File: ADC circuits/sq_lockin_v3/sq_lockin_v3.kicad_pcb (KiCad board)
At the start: 2 copper layers, 100 x 70 mm, 78 parts, among them J1 battery, J10 Conn_01x03_Male, J11 Conn_01x02_Male_2.54mm, J12 Conn_01x02_Male_2.54mm, J13 Conn_01x02_Male_2.54mm, J14 Conn_01x02_Male_2.54mm, J2 Conn_01x02_Male_2.54mm, J21 Conn_01x02_Male_2.54mm, J22 Conn_01x03_Female, J3 DB9_Female_MountingHoles, J4 Conn_01x02_Male_2.54mm, J5 Conn_01x02_Male_2.54mm, J6 receptacle, J7 Conn_01x03_Female, J8 USB_C_KoreanHroparts_6P, J9 receptacle, Q1 BSS84, Q2 2N7002, Q3 BSS84, Q4 2N7002, Q5 BSS84, Q6 2N7002, U10 LMP7715, U11 HX710C, U12 HX710C, U13 AQW212EHAX, U14 AQW212EHAX, U15 KAQY212S, U16 AQW212EHAX, U17 AQW212EHAX, U2 REF3320, U3 LP5907MFX-4.5, U4 LP5907MFX-3.3, U5 LMP7715, U6 LMP7715, U7 AQW212EHAX, U8 AQW212EHAX, U9 LMP7715

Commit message: Add power-two-wre and tweaks to sq_lockin_v3
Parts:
- removed C10, C11: 100nF, Capacitor_SMD:C_0603_1608Metric_Pad1.05x0.95mm_HandSolder
- removed J12, J14: Conn_01x02_Male_2.54mm, Connector_PinHeader_2.54mm:PinHeader_1x02_P2.54mm_Vertical
- removed U10, U9: LMP7715, Package_TO_SOT_SMD:TSOT-23-5
- removed U15: KAQY212S, 0my_footprints:SOP-4_L4.4-W4.0-P2.54-LS7.0-BL
- added C1: 100nF, Capacitor_SMD:C_0603_1608Metric_Pad1.05x0.95mm_HandSolder, F.Cu at (182.1, 102.1)
- added C15: 100nF, Capacitor_SMD:C_0603_1608Metric_Pad1.05x0.95mm_HandSolder, F.Cu at (181.6, 96.6)
- added C16: 100nF, Capacitor_SMD:C_0603_1608Metric_Pad1.05x0.95mm_HandSolder, F.Cu at (193.6, 100.8)
- added C17: 100nF, Capacitor_SMD:C_0603_1608Metric_Pad1.05x0.95mm_HandSolder, F.Cu at (187.5, 107.8)
- added D1: LBAT54HT1G, Diode_SMD:D_SOD-323, F.Cu at (172.2, 71.6)
- added D2: LBAT54HT1G, Diode_SMD:D_SOD-323, F.Cu at (172.2, 69.2)
- added R25: 100, Resistor_SMD:R_0603_1608Metric_Pad1.05x0.95mm_HandSolder, F.Cu at (186.6, 97.0)
- added R26: 10, Resistor_SMD:R_0603_1608Metric_Pad1.05x0.95mm_HandSolder, F.Cu at (190.9, 106.6)
- added R27: 10K, Resistor_SMD:R_0603_1608Metric_Pad1.05x0.95mm_HandSolder, F.Cu at (183.6, 107.8)
- added R28: 10K, Resistor_SMD:R_0603_1608Metric_Pad1.05x0.95mm_HandSolder, F.Cu at (181.4, 110.7)
- added U1: LMP7715, Package_TO_SOT_SMD:TSOT-23-5, F.Cu at (179.5, 104.7)
- added U18: LMP7715, Package_TO_SOT_SMD:TSOT-23-5, F.Cu at (179.5, 99.3)
- added U19: AD623, Package_SO:SOIC-8_3.9x4.9mm_P1.27mm, F.Cu at (188.4, 101.9)
- added U20: LMP7715, Package_TO_SOT_SMD:TSOT-23-5, F.Cu at (185.3, 110.5)
- J3: footprint Connector_Dsub:DSUB-9_Female_Horizontal_P2.77x2.84mm_EdgePinOffset4.94mm_Housed_MountingHolesOffset7.48mm -> 0my_footprints:DSUB-TH_DS1037-09FNAKT74-0CC
- U2: footprint Package_TO_SOT_SMD:SOT-23 -> Package_TO_SOT_SMD:SOT-323_SC-70
- moved J13 71.7 mm to (190.9, 97.0), turned to 90 degrees
- moved Q1 42.6 mm to (159.2, 91.7)
- moved Q2 42.6 mm to (163.6, 91.7)
- moved Q3 31.8 mm to (157.9, 114.9)
- moved Q4 31.8 mm to (162.4, 114.9)
- moved Q6 27.8 mm to (146.9, 104.1), turned to 270 degrees
- moved Q5 24.4 mm to (146.9, 108.0)
- moved C6 13.8 mm to (138.4, 61.0), turned to 90 degrees
- moved J7 9.28 mm to (207.4, 109.6)
- moved U2 9.15 mm to (135.7, 61.0), turned to 90 degrees
- moved J5 7.10 mm to (143.0, 81.4)
- moved C5 5.85 mm to (132.7, 60.9), turned to 90 degrees
- moved C12 5.83 mm to (197.5, 105.6)
- moved C14 5.83 mm to (207.2, 102.6)
- moved C13 5.83 mm to (197.3, 101.5)
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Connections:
- net /sheet624D2E56/in+ renamed /Sheet6275CBF8/in+
- net /sheet624D2E56/in- renamed /Sheet6275CBF8/in-
- C5 pad 2: Net-(C5-Pad2) -> GND
- C6 pad 2: Net-(C5-Pad2) -> GND
- J1 pad 1: Net-(C2-Pad1) -> Net-(D2-Pad2)
- J13 pad 2: /sheet624D2E58/ctrl- -> Net-(J13-Pad2)
- Q1 pad 3: Net-(J12-Pad1) -> /Sheet624B5D4E/ctrl-
- Q2 pad 3: Net-(J12-Pad1) -> /Sheet624B5D4E/ctrl-
- Q3 pad 3: Net-(J13-Pad1) -> /sheet624D2E58/ctrl-
- Q4 pad 3: Net-(J13-Pad1) -> /sheet624D2E58/ctrl-
- Q5 pad 3: Net-(J14-Pad1) -> /sheet6256EE2A/ctrl-
- Q6 pad 3: Net-(J14-Pad1) -> /sheet6256EE2A/ctrl-
- R11 pad 1: Net-(R11-Pad1) -> Net-(J5-Pad2)
- R12 pad 1: Net-(R12-Pad1) -> Net-(J5-Pad1)
- R12 pad 2: Net-(R11-Pad1) -> Net-(J5-Pad2)
- R13 pad 2: Net-(R12-Pad1) -> Net-(J5-Pad1)
- R9 pad 1: Net-(R12-Pad1) -> Net-(J5-Pad1)
- U2 pad 3: Net-(C5-Pad2) -> GND
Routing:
- net VCC: track 69.4 -> 288.1 mm, vias 4 -> 14
- net /vref: track 7.35 -> 155.5 mm, vias 2 -> 5
- net /V-: track 0.27 -> 81.0 mm, vias 0 -> 2
- net /V+: track 0.16 -> 68.3 mm, vias 0 -> 1
- net /I+: track 17.2 -> 78.8 mm, vias 2 -> 3
- net /sheet6256EE2A/ctrl-: track 0.00 -> 54.7 mm
- net /sheet6256EE2A/ctrl+: track 0.00 -> 53.2 mm, vias 0 -> 2
- net +4V: track 10.2 -> 45.6 mm
- net GND: track 72.6 -> 107.3 mm, vias 2 -> 6
- net /Sheet624B5D4E/in+: track 19.6 -> 52.2 mm, vias 2 -> 3
- net /I-: track 3.26 -> 35.8 mm
- net Net-(J3-Pad0): track 0.00 -> 32.0 mm
- net Net-(C4-Pad1): track 28.7 -> 58.8 mm
- net /Sheet6275CBF8/in+: track 0.00 -> 29.9 mm
- net /Sheet621A3D16/in+: track 5.85 -> 31.0 mm
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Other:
- board text added: "sq_lockin_v3 4/2022"
- board text removed: "ADC preamp test CS5530 test 2/2022"

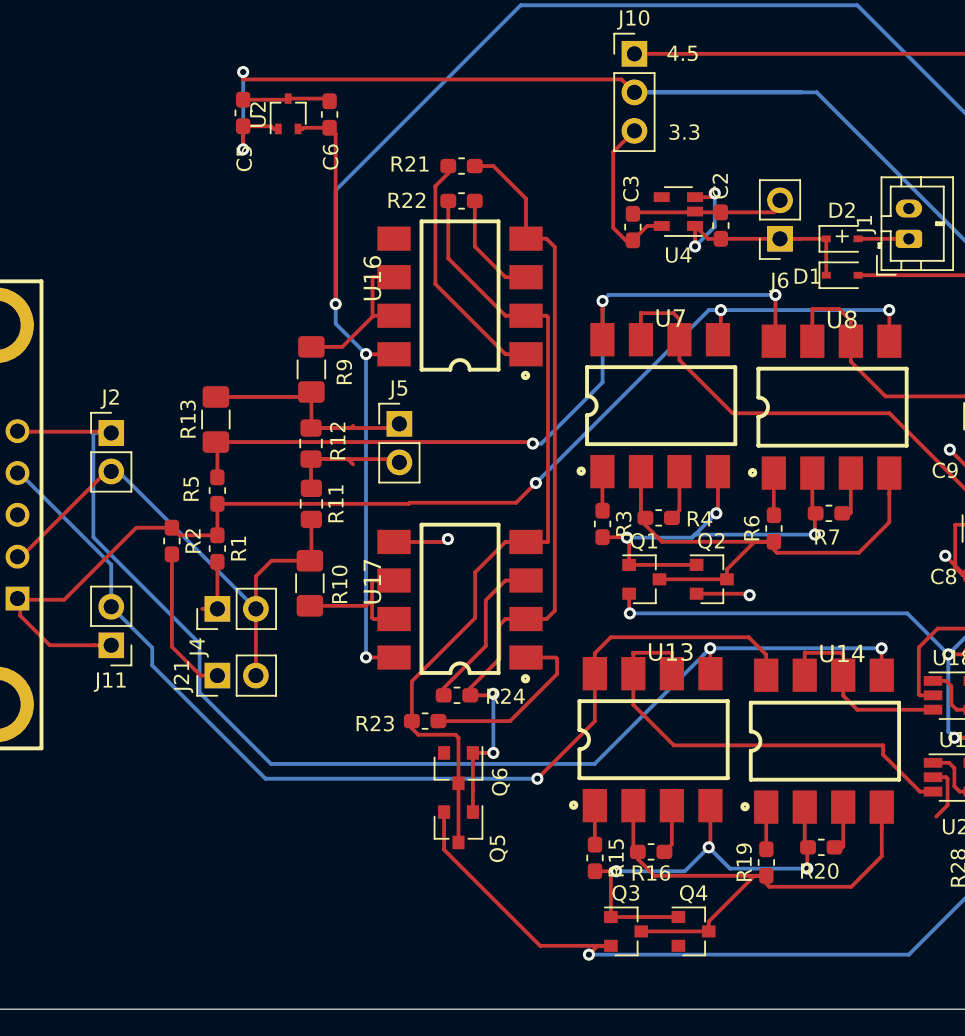
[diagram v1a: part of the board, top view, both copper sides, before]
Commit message: add uart mux versions
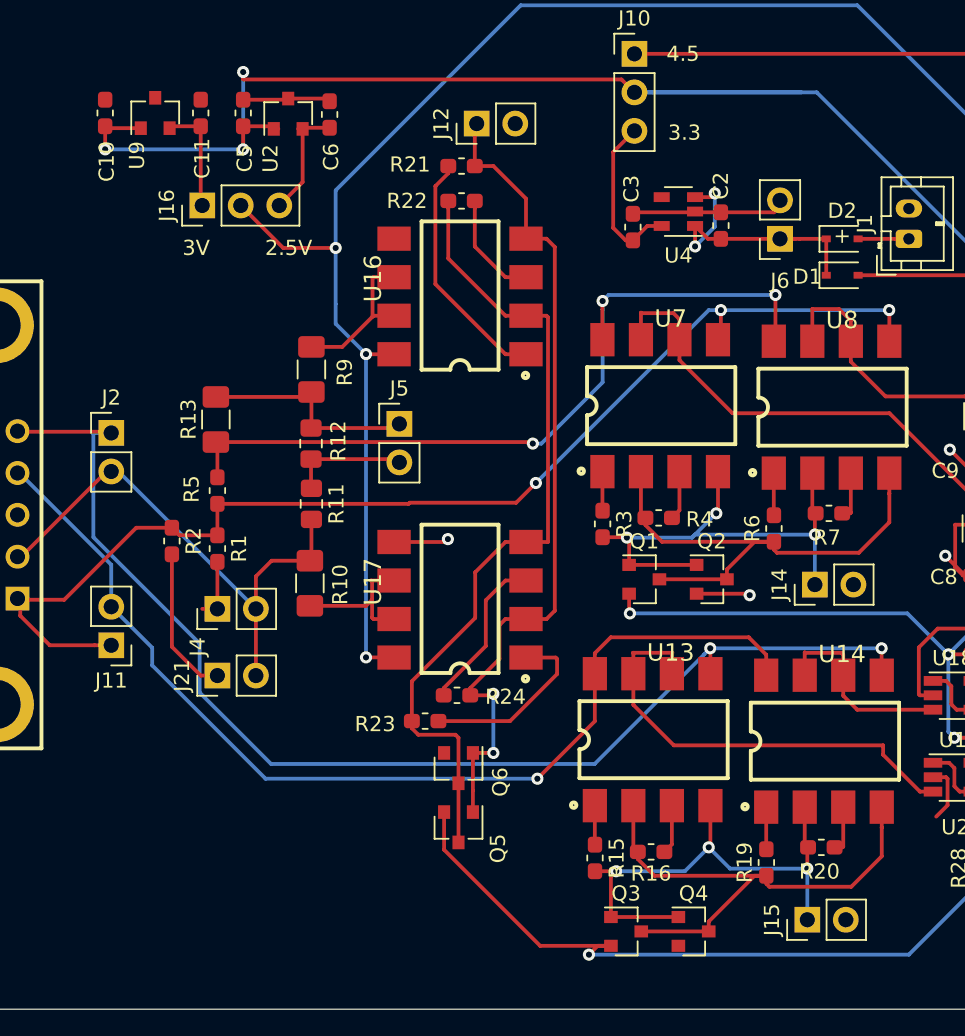
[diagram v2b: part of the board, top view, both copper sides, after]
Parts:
- added C10: 1uF, Capacitor_SMD:C_0603_1608Metric_Pad1.05x0.95mm_HandSolder, F.Cu at (123.6, 60.9)
- added C11: 1uF, Capacitor_SMD:C_0603_1608Metric_Pad1.05x0.95mm_HandSolder, F.Cu at (129.9, 60.9)
- added J12: Conn_01x02_Male_2.54mm, Connector_PinHeader_2.54mm:PinHeader_1x02_P2.54mm_Vertical, F.Cu at (148.1, 61.6)
- added J14: Conn_01x02_Male_2.54mm, Connector_PinHeader_2.54mm:PinHeader_1x02_P2.54mm_Vertical, F.Cu at (170.4, 92.0)
- added J15: Conn_01x02_Male_2.54mm, Connector_PinHeader_2.54mm:PinHeader_1x02_P2.54mm_Vertical, F.Cu at (169.9, 114.1)
- added J16: Conn_01x03_Male, Connector_PinHeader_2.54mm:PinHeader_1x03_P2.54mm_Vertical, F.Cu at (130.0, 67.0)
- added U9: REF3030, Package_TO_SOT_SMD:SOT-23, F.Cu at (126.9, 60.9)
- U2: value REF3320 -> REF3325; footprint Package_TO_SOT_SMD:SOT-323_SC-70 -> Package_TO_SOT_SMD:SOT-23
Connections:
- C6 pad 1: /vref -> /vref1
- U2 pad 2: /vref -> /vref1
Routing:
- net VCC: track 288.1 -> 301.2 mm, vias 14 -> 15
- net /vref1: track 0.00 -> 7.80 mm
- net /vref2: track 0.00 -> 7.37 mm
- net /vref: track 155.5 -> 149.0 mm
- net /sheet624D2E58/ctrl+: track 29.8 -> 33.2 mm
- net /Sheet624B5D4E/ctrl+: track 29.6 -> 32.9 mm
- net Net-(J5-Pad2): track 11.0 -> 8.11 mm
- net /sheet6256EE2A/ctrl+: track 53.2 -> 56.1 mm
- net Net-(J5-Pad1): track 18.5 -> 15.7 mm
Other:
- board text added: "2.5V"
- board text added: "3V"
